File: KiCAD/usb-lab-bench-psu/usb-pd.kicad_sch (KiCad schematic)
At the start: 5 parts, among them J13 USB_PD_Receptacle, U1 USBLC6-2SC6

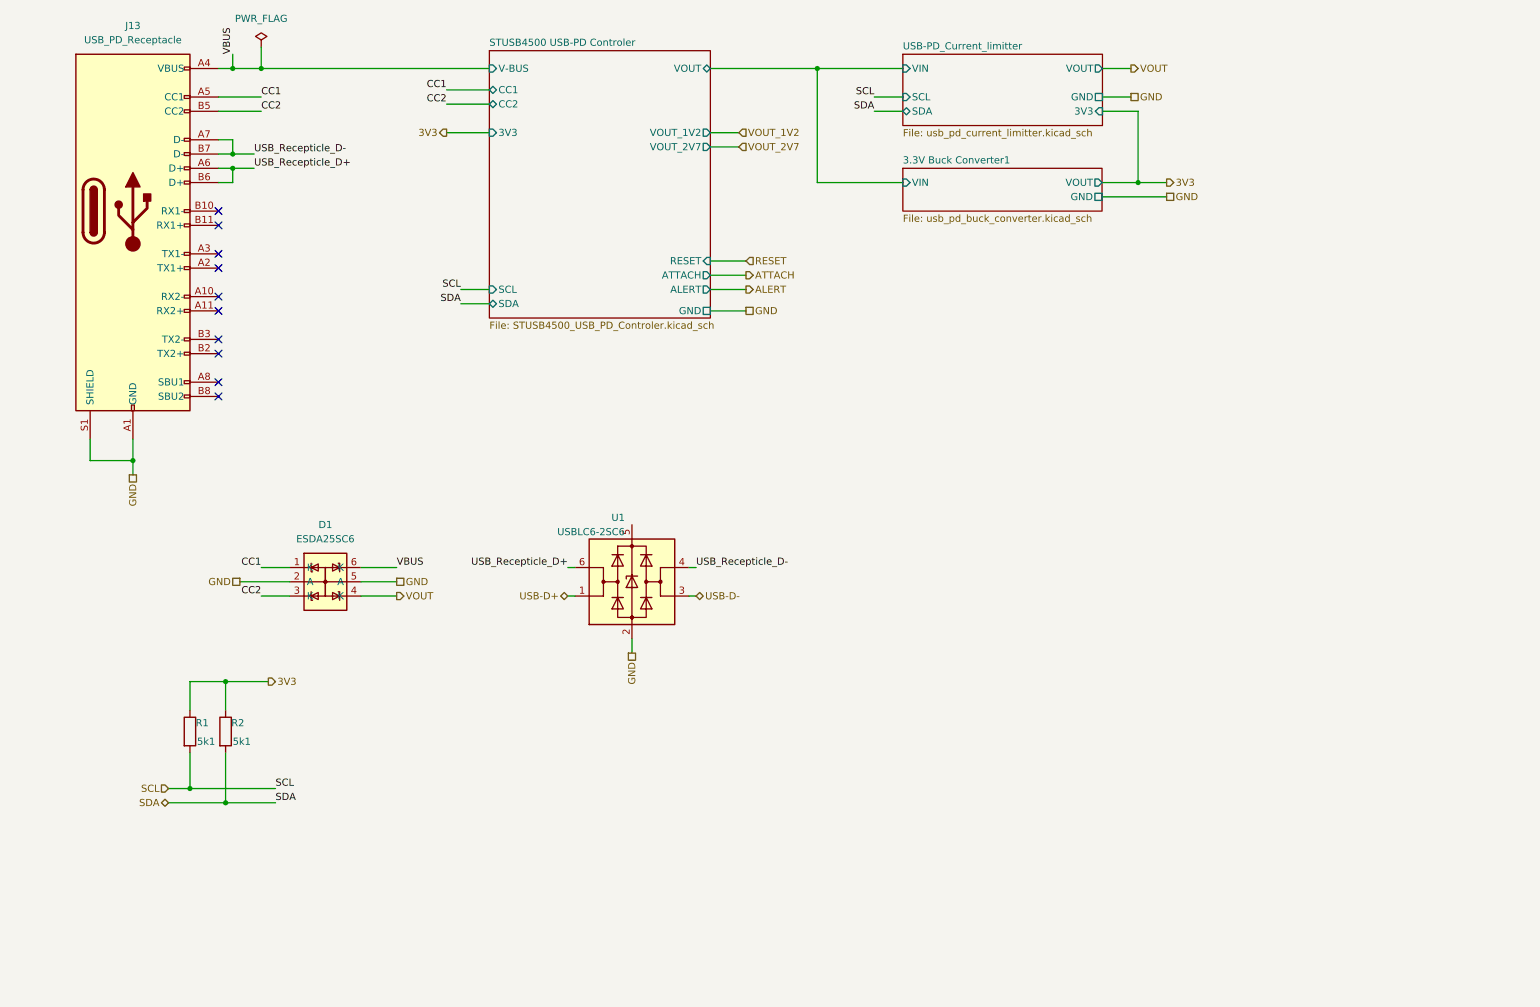
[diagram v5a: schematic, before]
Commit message: tweaked design of current limiter, added GPIO expander to USB-PD circuit
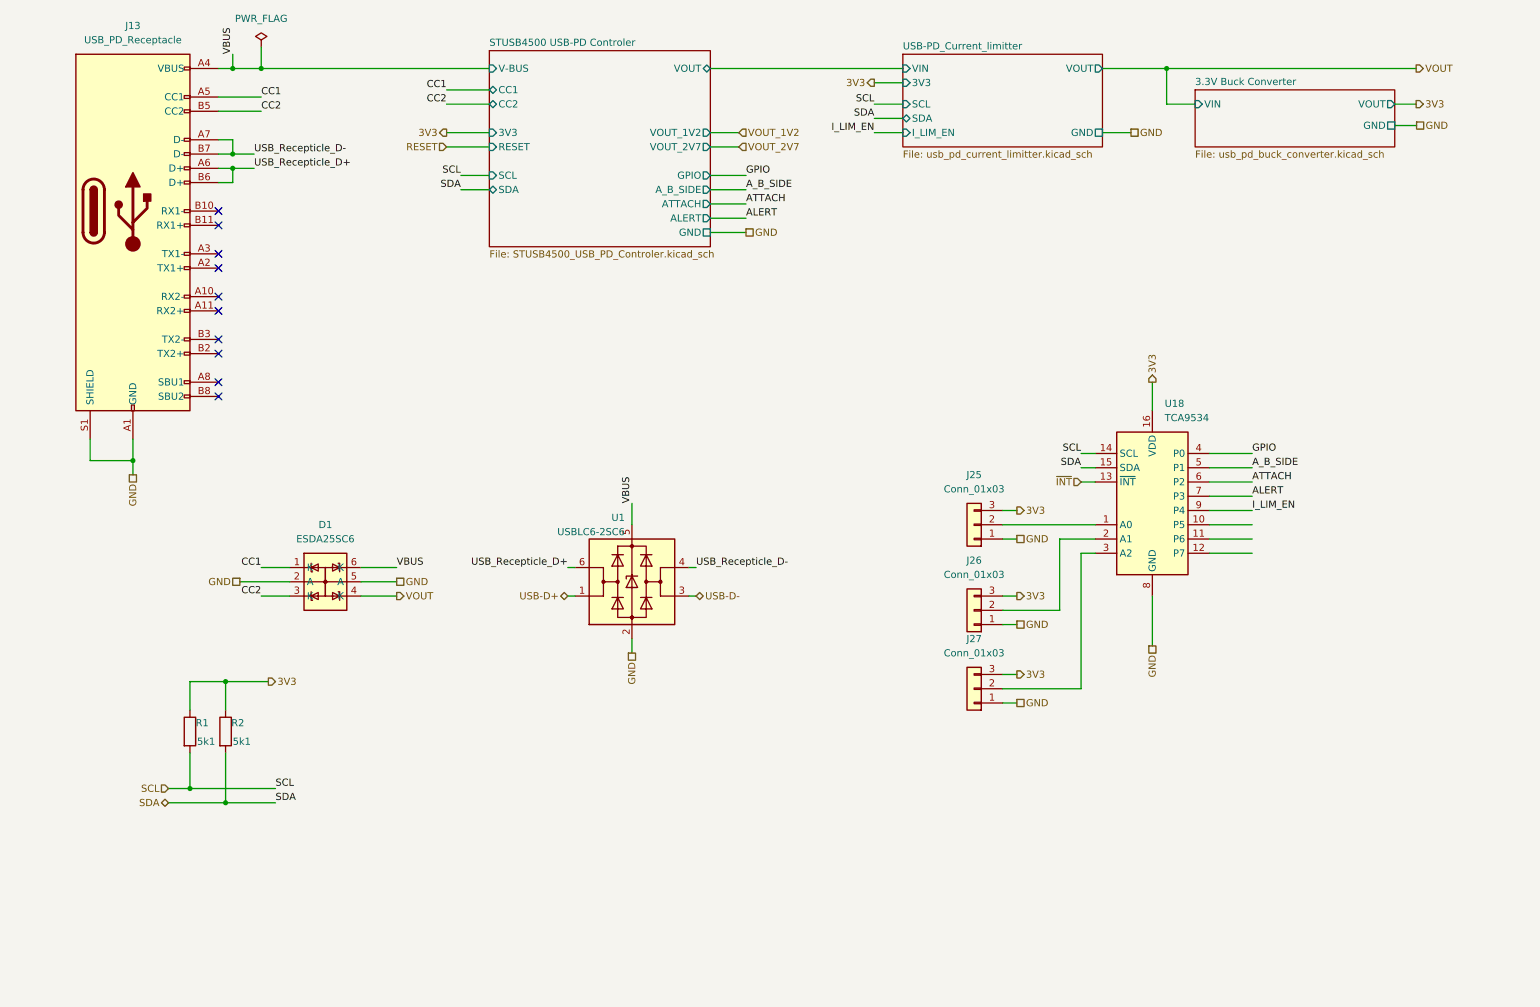
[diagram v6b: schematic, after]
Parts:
- added J25, J26, J27: Conn_01x03, symbol Connector_Generic:Conn_01x03
- added U18: TCA9534, symbol Interface_Expansion:TCA9534
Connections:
- net 3V3: now also J25.3 (Pin_3), J26.3 (Pin_3), J27.3 (Pin_3), U18.16 (VDD)
- net ALERT: now also U18.7 (P3)
- net ATTACH: now also U18.6 (P2)
- net GND: now also J25.1 (Pin_1), J26.1 (Pin_1), J27.1 (Pin_1), U18.8 (GND)
- net SCL: now also U18.14 (SCL)
- net SDA: now also U18.15 (SDA)
- net VBUS: now also U1.5 (VBUS)
- new net: J25.2 (Pin_2), U18.1 (A0)
- new net: J26.2 (Pin_2), U18.2 (A1)
- new net: J27.2 (Pin_2), U18.3 (A2)
- new net A_B_SIDE: U18.5 (P1)
- new net GPIO: U18.4 (P0)
- new net I_LIM_EN: U18.9 (P4)
- new net ~{INT}: U18.13 (~{INT})
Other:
- sheet 3.3V Buck Converter1 renamed 3.3V Buck Converter
- sheet STUSB4500 USB-PD Controler ports: added A_B_SIDE, GPIO; removed none
- sheet USB-PD_Current_limitter ports: added I_LIM_EN; removed none
